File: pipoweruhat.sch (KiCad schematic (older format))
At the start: 38 parts, among them J1 GPIO_CONNECTOR, J2 car battery connection, U1 LM2596S-5, U2 SFH6156-2T, U3 PIC10F200-IOT, U4 CPC1017N, U5 DS1307Z+, U9 CAT24C32WI, X5 MC-306

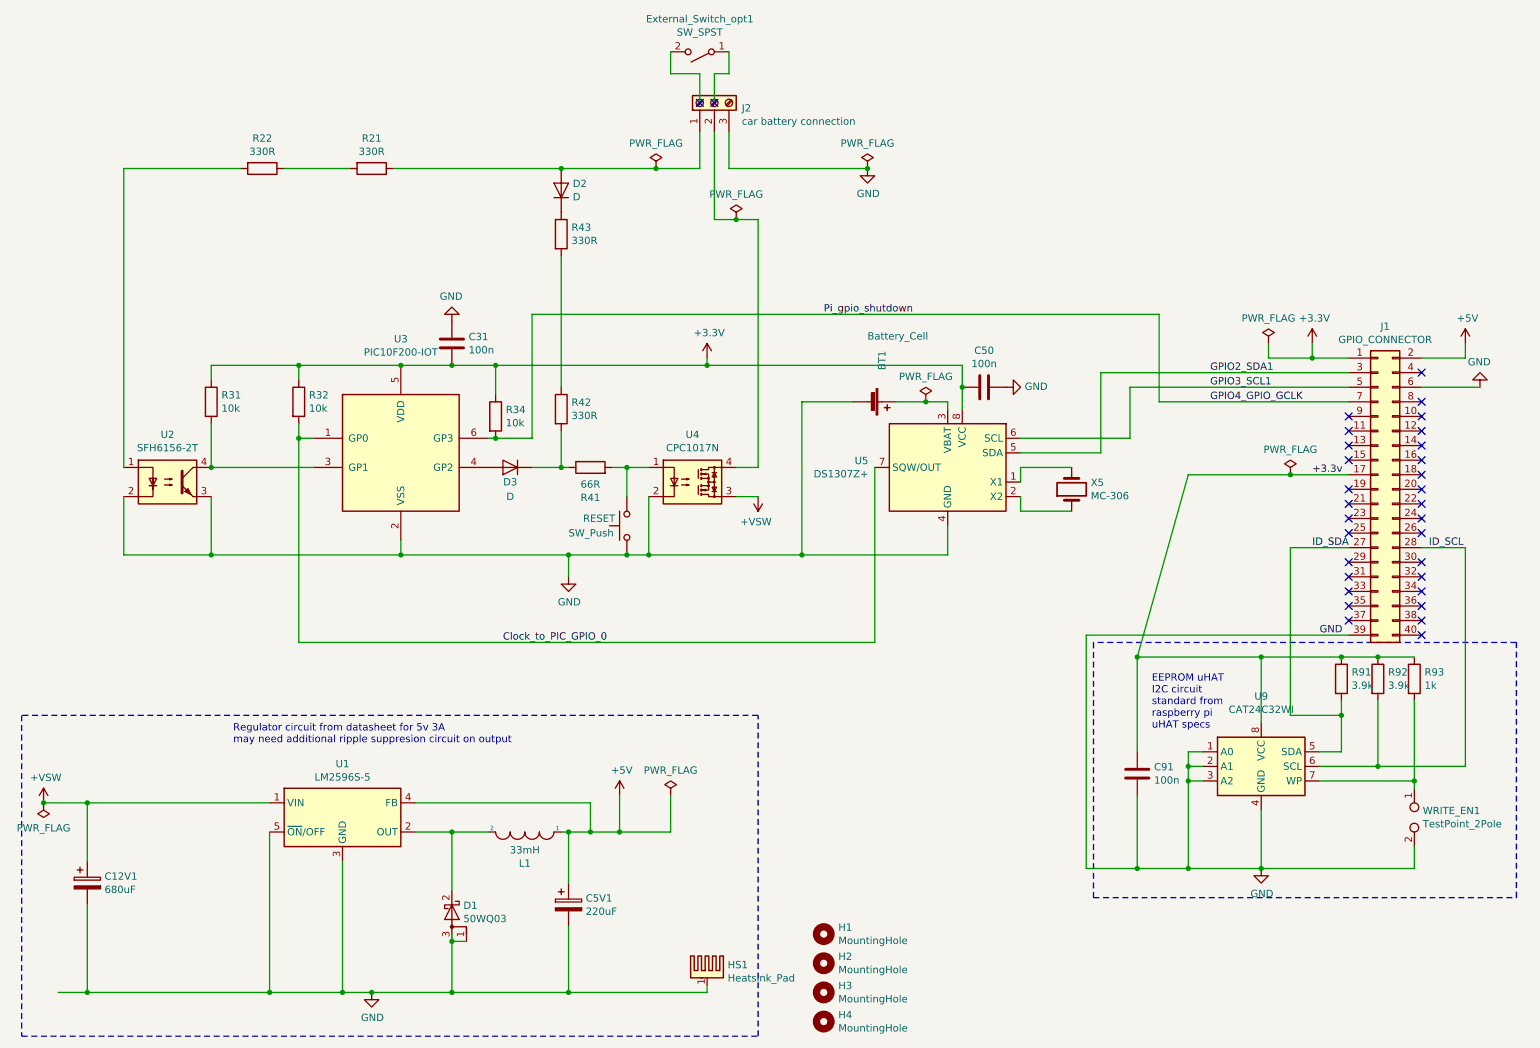
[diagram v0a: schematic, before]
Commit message: schematic done
footprints assigned for tht parts
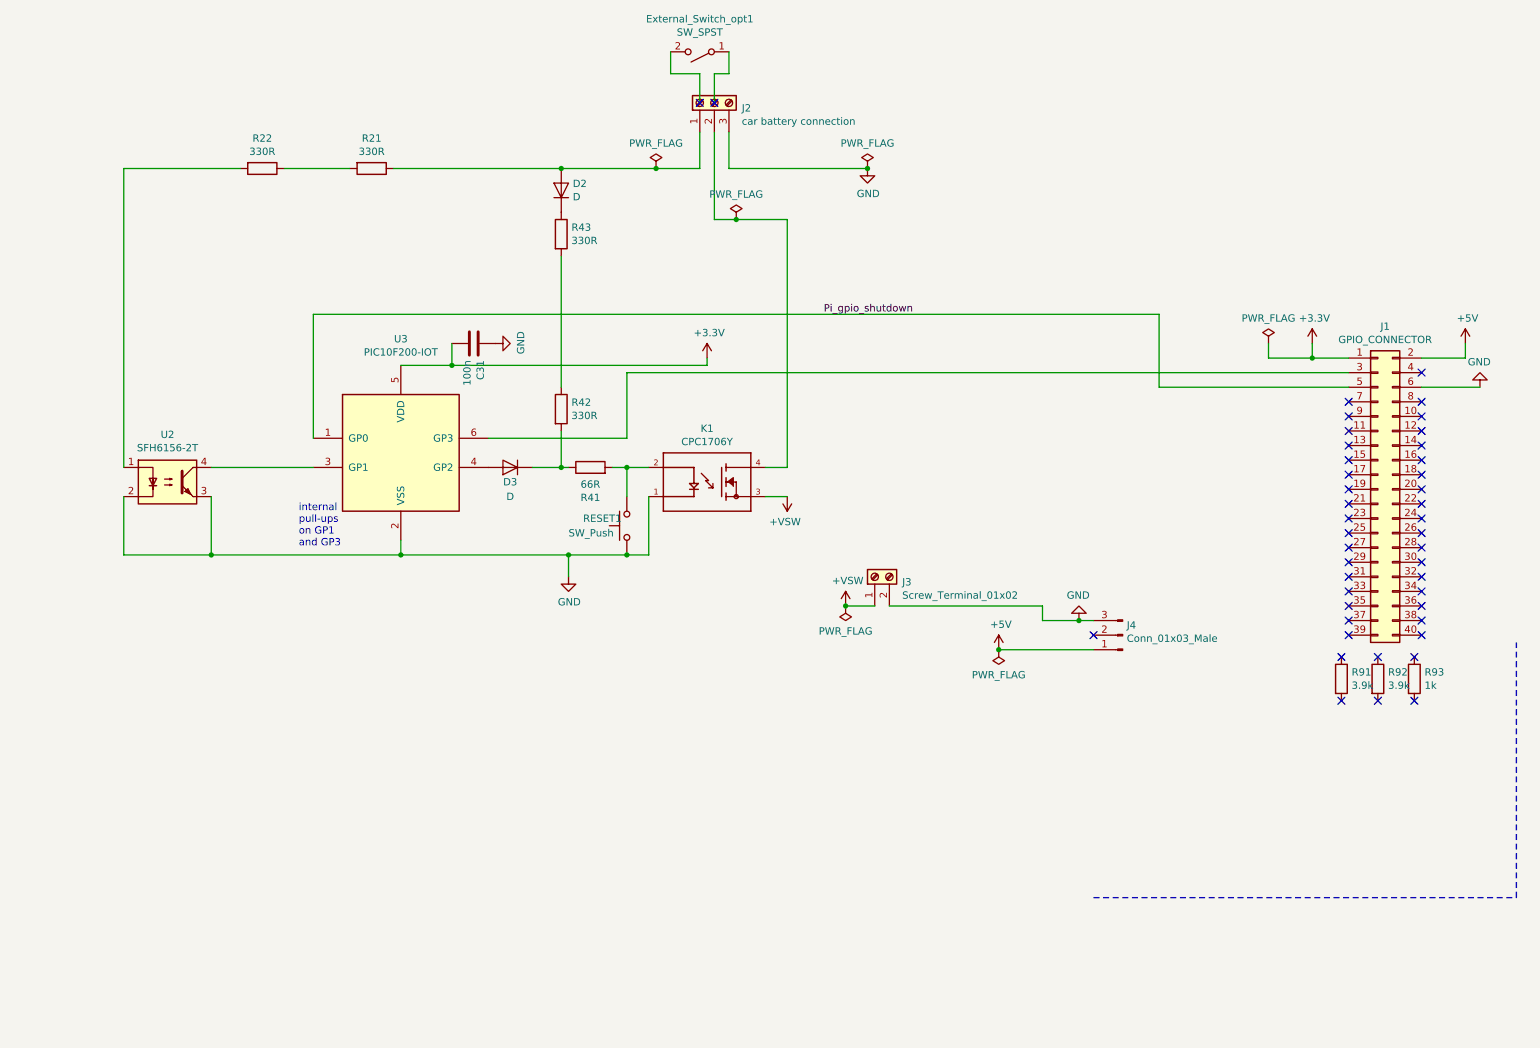
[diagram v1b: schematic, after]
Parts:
- removed BT1: Battery_Cell, Battery:BatteryHolder_Keystone_3000_1x12mm, symbol Device:Battery_Cell
- removed C12V1: 680uF, Capacitor_SMD:CP_Elec_16x17.5, symbol Device:CP
- removed C50, C91: 100n, Capacitor_SMD:C_0805_2012Metric_Pad1.15x1.40mm_HandSolder, symbol Device:C
- removed C5V1: 220uF, Capacitor_Tantalum_SMD:CP_EIA-6032-20_AVX-F_Pad2.25x2.35mm_HandSolder, symbol Device:CP
- removed D1: 50WQ03, Package_TO_SOT_SMD:TO-252-2, symbol Device:D_Schottky_AKA
- removed H1, H2, H3, H4: MountingHole, lib:MountingHole_2.7mm_M2.5_uHAT_RPi, symbol Mechanical:MountingHole
- removed HS1: Heatsink_Pad, HSINK_7109DG:HSINK_7109DG, symbol Mechanical:Heatsink_Pad
- removed L1: 33mH, Inductor_SMD:L_12x12mm_H6mm, symbol pspice:INDUCTOR
- removed R31, R32, R34: 10k, Resistor_SMD:R_0805_2012Metric_Pad1.15x1.40mm_HandSolder, symbol Device:R
- removed U1: LM2596S-5, Package_TO_SOT_SMD:TO-263-5_TabPin3, symbol Regulator_Switching:LM2596S-5
- removed U4: CPC1017N, Package_SO:SOP-4_3.8x4.1mm_P2.54mm, symbol Relay_SolidState:CPC1017N
- removed U5: DS1307Z+, Package_SO:SOIC-8_3.9x4.9mm_P1.27mm, symbol Timer_RTC:DS1307Z+
- removed U9: CAT24C32WI, Package_SO:SOIC-8_3.9x4.9mm_P1.27mm, symbol Memory_EEPROM:CAT24C128
- removed WRITE_EN1: TestPoint_2Pole, TestPoint:TestPoint_2Pads_Pitch2.54mm_Drill0.8mm, symbol Connector:TestPoint_2Pole
- removed X5: MC-306, Crystal:Crystal_SMD_SeikoEpson_MC306-4Pin_8.0x3.2mm_HandSoldering, symbol Device:Crystal
- added J3: Screw_Terminal_01x02, TerminalBlock_TE-Connectivity:TerminalBlock_TE_282834-2_1x02_P2.54mm_Horizontal, symbol Connector:Screw_Terminal_01x02
- added J4: Conn_01x03_Male, Connector_PinHeader_2.54mm:PinHeader_1x03_P2.54mm_Horizontal, symbol Connector:Conn_01x03_Male
- added K1: CPC1706Y, CPC1706Y:RELAY_CPC1706Y, symbol CPC1706Y:CPC1706Y
- C31: footprint Capacitor_SMD:C_0805_2012Metric_Pad1.15x1.40mm_HandSolder -> Package_DIP:DIP-8_W7.62mm_Socket
- D2, D3: footprint (none) -> Diode_THT:D_DO-35_SOD27_P7.62mm_Horizontal
- J2: footprint (none) -> TerminalBlock_TE-Connectivity:TerminalBlock_TE_282834-3_1x03_P2.54mm_Horizontal
- R21, R22, R41, R42, R43: footprint Resistor_SMD:R_0805_2012Metric_Pad1.15x1.40mm_HandSolder -> Resistor_THT:R_Axial_DIN0309_L9.0mm_D3.2mm_P12.70mm_Horizontal
- renumbered RESET to RESET1
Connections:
- net GPIO3_SCL1 is gone; now on net Pi_gpio_shutdown: J1.5 (Pin_5)
- net +5V: now also J4.1 (Pin_1)
- net +VSW: now also J3.1 (Pin_1), K1.3
- net GND: now also J3.2 (Pin_2), J4.3 (Pin_3), K1.1; no longer J1.39 (Pin_39)
- net at J2.2 (Pin_2): now also K1.4
- net at R41.2, RESET1.2: now also K1.2
- removed net +3.3v: J1.17 (Pin_17), R91.1, R92.1, R93.1
- net Clock_to_PIC_GPIO_0 renamed Pi_gpio_shutdown
- net GPIO2_SDA1: no longer names the net of J1.3 (Pin_3)
- net GPIO2_SDA1: now also U3.6 (GP3)
- net GPIO4_GPIO_GCLK: no longer names the net of J1.7 (Pin_7)
- net GPIO4_GPIO_GCLK: no longer U3.6 (GP3)
- net ID_SCL: no longer names the net of J1.28 (Pin_28)
- net ID_SCL: no longer R92.2
- net ID_SDA: no longer names the net of J1.27 (Pin_27)
- net ID_SDA: no longer R91.2
- no-connect marks 32 -> 44
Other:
- note added: "internal \npull-ups \non GP1 \nand GP3"
- note removed: "EEPROM uHAT\nI2C circuit\nstandard from\nraspberry pi \nuHAT specs"
- note removed: "Regulator circuit from datasheet for 5v 3A\nmay need additional ripple suppresion circuit on output"
- moved on the sheet: C31
